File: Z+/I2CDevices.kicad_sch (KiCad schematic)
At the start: 33 parts, among them U4 ADM1176-1ARMZ-R7, U5 ADM1176-1ARMZ-R7, U6 NCV891330PD50R2G, U7 DRV8830DRC, U9 SunSensor

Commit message: Z- Board Files
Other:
- note added: "I2C ADDR 0x64 Install R68: 0x63"
- note added: "I2C ADDR 0x84 Install R67: 0x80"
- note added: "I2C ADDR 0x94 Install R66: 0x90"
- note removed: "I2C ADDR 0x64 Install R96: 0x63"
- note removed: "I2C ADDR 0x84 Install R94: 0x80"
- note removed: "I2C ADDR 0x94 Install R95: 0x90"
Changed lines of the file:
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@@
 		)
 	)
-	(text "I2C ADDR\n0x94\nInstall R95: 0x90"
+	(text "I2C ADDR\n0x94\nInstall R66: 0x90"
 		(exclude_from_sim no)
 		(at 75.438 131.826 0)
@@
 		)
 	)
-	(text "I2C ADDR\n0x84\nInstall R94: 0x80"
+	(text "I2C ADDR\n0x84\nInstall R67: 0x80"
 		(exclude_from_sim no)
 		(at 75.438 181.356 0)
@@
 		)
 	)
-	(text "I2C ADDR\n0x64\nInstall R96: 0x63"
+	(text "I2C ADDR\n0x64\nInstall R68: 0x63"
 		(exclude_from_sim no)
 		(at 185.166 147.32 0)

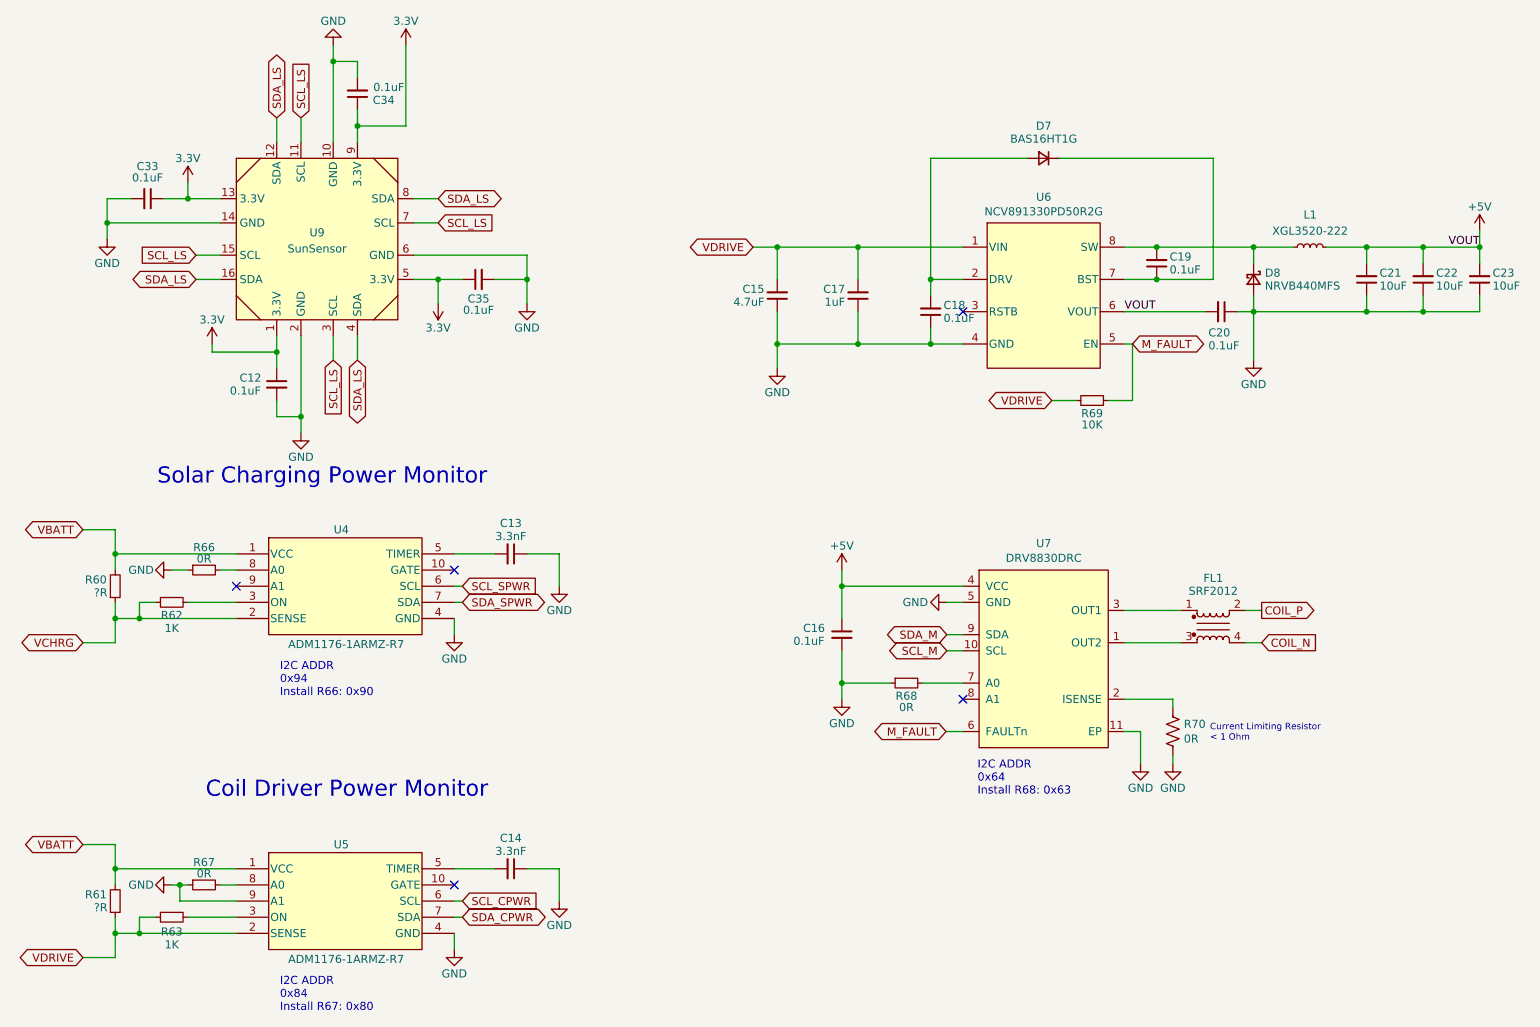
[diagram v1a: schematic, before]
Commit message: Added DRV8235, Quad Light Sensor, and refactored schematics
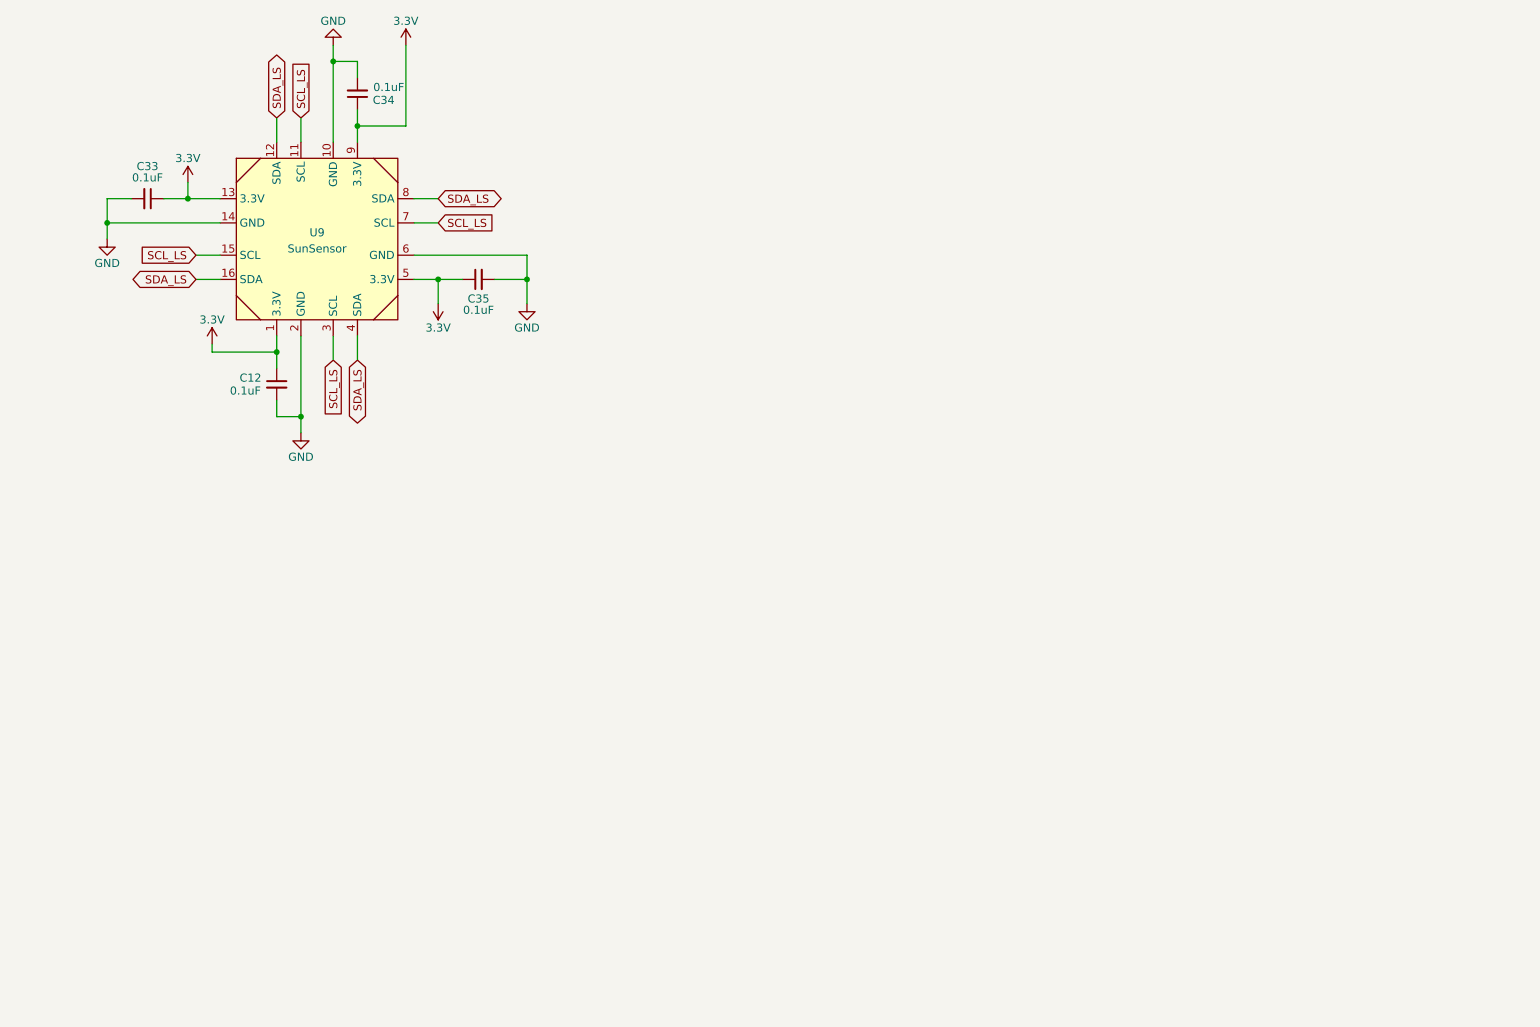
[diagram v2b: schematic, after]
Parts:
- removed C13, C14: 3.3nF, Capacitor_SMD:C_0603_1608Metric, symbol Device:C_Small
- removed C15: 4.7uF, Capacitor_SMD:C_1210_3225Metric, symbol Device:C_Small
- removed C16: 0.1uF, Capacitor_SMD:C_0805_2012Metric, symbol Device:C_Small
- removed C17: 1uF, Capacitor_SMD:C_0805_2012Metric, symbol Device:C_Small
- removed C18, C19, C20: 0.1uF, Capacitor_SMD:C_0603_1608Metric, symbol Device:C_Small
- removed C21, C22, C23: 10uF, Capacitor_SMD:C_1206_3216Metric, symbol Device:C_Small
- removed D7: BAS16HT1G, Diode_SMD:D_SOD-323, symbol Device:D_Small
- removed D8: NRVB440MFS, SolarPanels:NRVB440MFSWFT1G, symbol Device:D_Schottky_Small
- removed FL1: SRF2012, SolarPanels:SRF2012, symbol Device:Filter_EMI_CommonMode
- removed L1: XGL3520-222, SolarPanels:XGL3520, symbol Device:L_Small
- removed R60, R61: ?R, Resistor_SMD:R_2512_6332Metric, symbol Device:R_Small
- removed R62, R63: 1K, Resistor_SMD:R_0603_1608Metric, symbol Device:R_Small
- removed R66, R67, R68: 0R, Resistor_SMD:R_0603_1608Metric, symbol Device:R_Small
- removed R69: 10K, Resistor_SMD:R_0603_1608Metric, symbol Device:R_Small
- removed R70: 0R, Resistor_SMD:R_0603_1608Metric, symbol Device:R_US
- removed U4, U5: ADM1176-1ARMZ-R7, Package_SO:MSOP-10_3x3mm_P0.5mm, symbol Mainboard:ADM1176-1ARMZ-R7
- removed U6: NCV891330PD50R2G, Package_SO:SOIC-8-1EP_3.9x4.9mm_P1.27mm_EP2.514x3.2mm, symbol SolarPanels:NCV891330PD50R2G
- removed U7: DRV8830DRC, Package_SON:VSON-10-1EP_3x3mm_P0.5mm_EP1.65x2.4mm, symbol mainboard:DRV8830DRC
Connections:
- no-connect marks 5 -> 0
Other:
- note removed: "Coil Driver Power Monitor"
- note removed: "Current Limiting Resistor < 1 Ohm"
- note removed: "I2C ADDR 0x64 Install R68: 0x63"
- note removed: "I2C ADDR 0x84 Install R67: 0x80"
- note removed: "I2C ADDR 0x94 Install R66: 0x90"
- note removed: "Solar Charging Power Monitor"
